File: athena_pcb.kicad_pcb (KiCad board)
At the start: 2 copper layers, 41.6 x 23.5 mm, 34 parts, among them J2 Conn_01x04, SW1 SW_Push, U1 NRF5340-QKAA-R7, U2 BME280, Y1 32MHz, Y2 32.768kHz

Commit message: Polishing layout
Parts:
- added TP3: TestPoint, TestPoint:TestPoint_Pad_D1.0mm, F.Cu at (99.0, 96.8)
- added TP4: TestPoint, TestPoint:TestPoint_Pad_D1.0mm, F.Cu at (108.8, 96.8)
- moved R1 1.78 mm to (102.6, 92.9)
- moved D1 1.77 mm to (103.1, 91.5)
- moved C9 0.30 mm to (118.0, 95.4)
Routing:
- net VDD: track 165.1 -> 187.1 mm, vias 2 -> 3
- net GND: track 32.2 -> 40.2 mm, vias 15 -> 21
- net unconnected-(U1D-P1.08-PadAL23): track 1.25 -> 0.00 mm
- net /P0.02: track 21.0 -> 22.2 mm
- net /SCK_SCL: track 23.9 -> 24.7 mm
- net /P0.03: track 10.7 -> 10.1 mm
- net /CSB: track 23.2 -> 23.8 mm
- net /SDI_SDA: track 23.3 -> 23.9 mm
- net /SDO: track 25.3 -> 25.8 mm

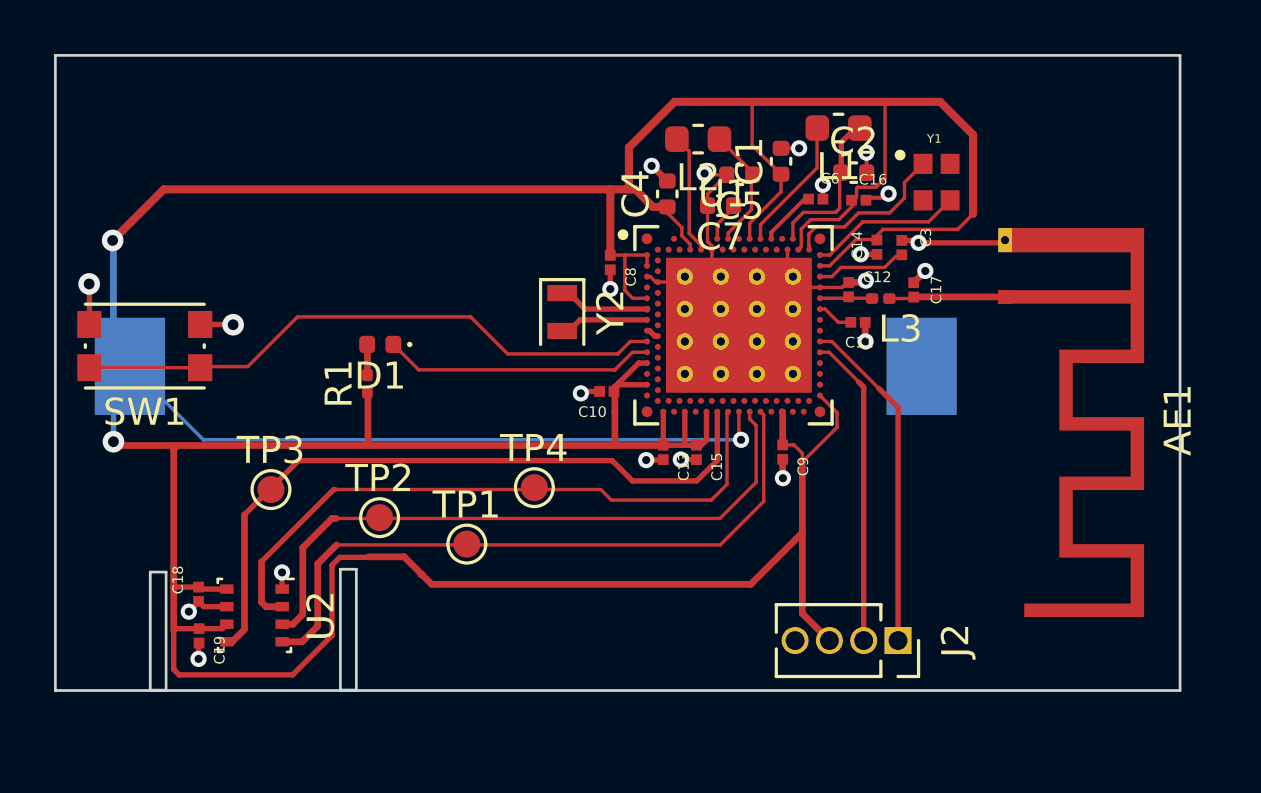
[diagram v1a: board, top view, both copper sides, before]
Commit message: Updated Header pinout, added ground pours to PCB
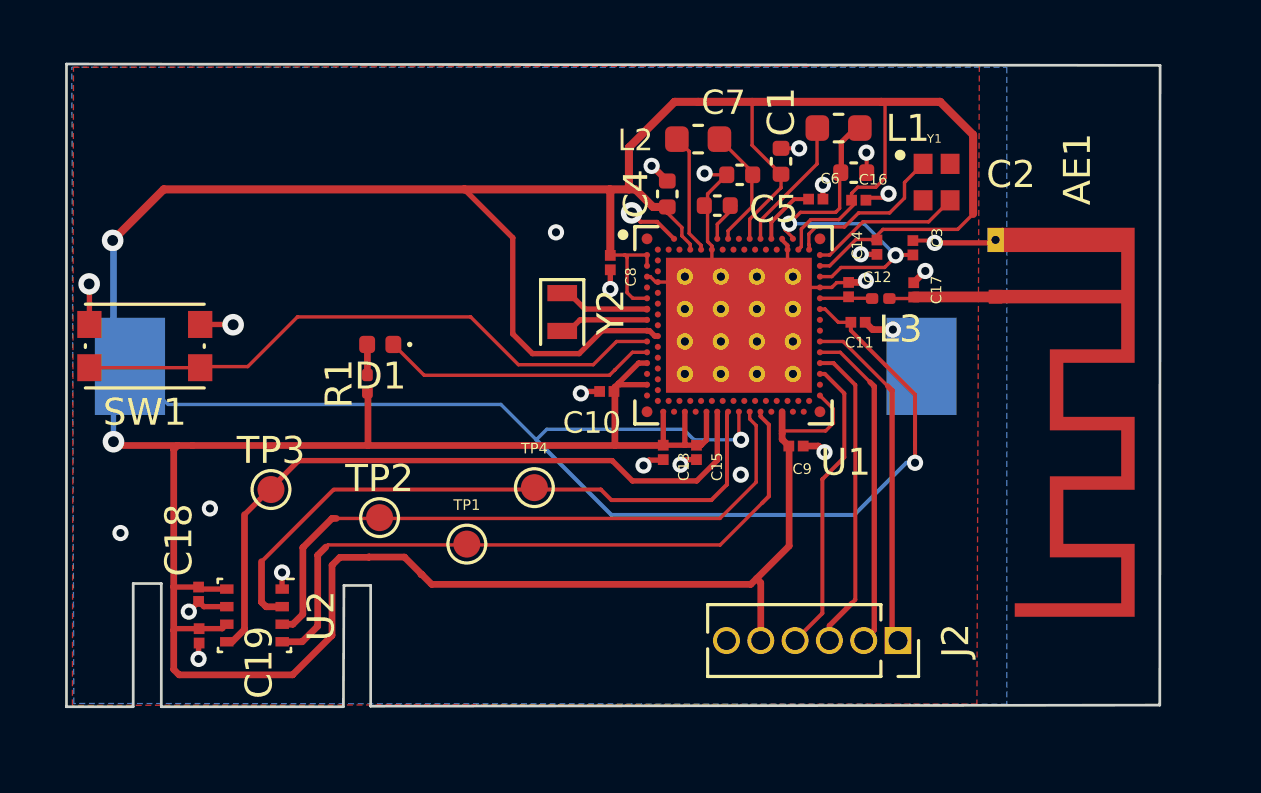
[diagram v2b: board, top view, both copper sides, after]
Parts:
- J2: footprint Connector_PinSocket_1.27mm:PinSocket_1x04_P1.27mm_Vertical -> Connector_PinSocket_1.27mm:PinSocket_1x06_P1.27mm_Vertical
- moved C9 0.54 mm to (118.4, 95.2), turned to 0 degrees
- moved C3 0.41 mm to (122.8, 87.9)
- moved AE1 0.35 mm to (125.8, 89.7)
- moved C7 0.12 mm to (115.5, 86.3)
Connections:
- J2 pad 3: VDD -> /RESETN
- J2 pad 4: GND -> /P0.28
- U1 pad AC31: unconnected-(U1B-~{RESET}-PadAC31) -> /RESETN
- U1 pad AE31: unconnected-(U1C-P0.28/AIN7-PadAE31) -> /P0.28
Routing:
- net VDD: track 187.1 -> 218.6 mm, vias 3 -> 4
- net /RESETN: track 0.00 -> 11.5 mm
- net /P0.28: track 0.00 -> 11.1 mm
- net Net-(U1A-DECR): track 8.84 -> 14.3 mm, vias 0 -> 2
- net GND: track 40.2 -> 43.3 mm, vias 21 -> 26
- net /SWDIO: track 11.5 -> 12.1 mm
- added copper zone on B.Cu, net GND
- added copper zone on F.Cu, net GND
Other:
- board size 41.6 x 23.5 mm -> 40.5 x 23.8 mm

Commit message: Changes from the review
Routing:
- net VDD: track 218.6 -> 167.2 mm, vias 4 -> 7
- net GND: track 43.3 -> 38.8 mm, vias 26 -> 25

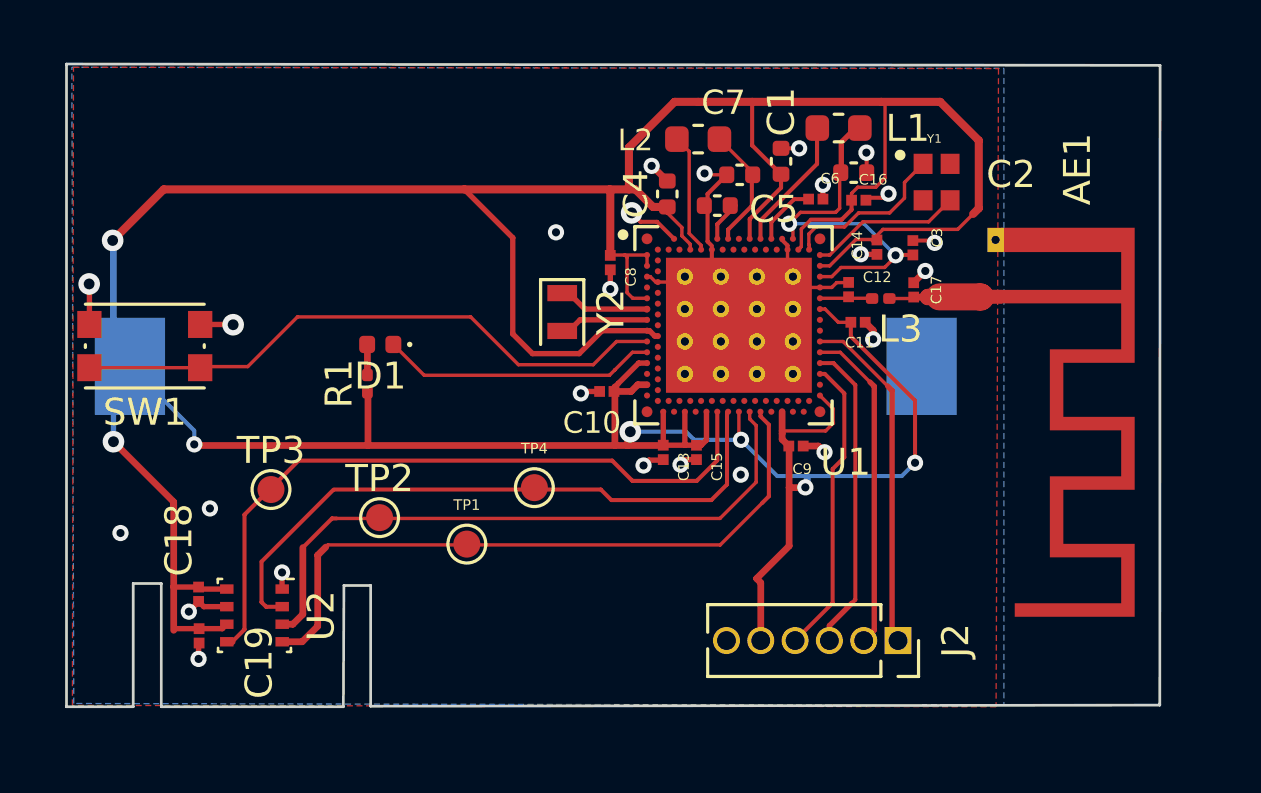
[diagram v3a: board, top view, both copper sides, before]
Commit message: Added items in the BOM
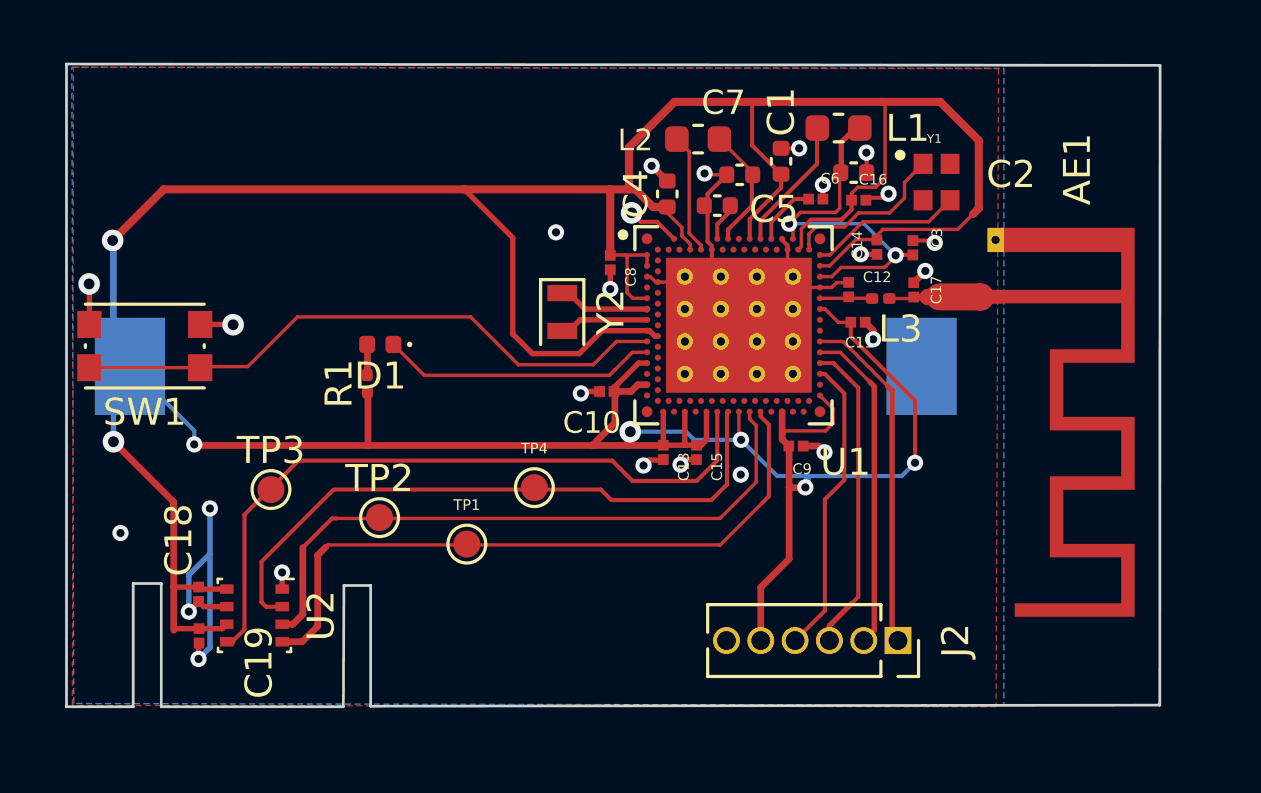
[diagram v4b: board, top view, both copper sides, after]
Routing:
- net GND: track 38.8 -> 47.0 mm
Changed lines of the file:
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@@
       (net 1 "VDD") (pinfunction "+") (pintype "passive"))
     (pad "2" smd rect (at 14.65 0 180) (size 2.6 3.6) (layers "B.Cu" "B.Paste" "B.Mask")
-      (net 2 "GND") (pinfunction "-") (pintype "passive"))
+      (net 2 "GND") (pinfunction "-") (pintype "passive") (zone_connect 1))
     (model "${KICAD6_3DMODEL_DIR}/Battery.3dshapes/BatteryHolder_Keystone_1060_1x2032.wrl"
       (offset (xyz 0 0 0))
@@
   (segment (start 111.2695 90.94) (end 110.4195 91.79) (width 0.2) (layer "F.Cu") (net 1))
   (segment (start 120.5 86.46283) (end 120.5 86.11) (width 0.1524) (layer "F.Cu") (net 1))
+  (segment (start 117.14 102.41) (end 117.14 100.44) (width 0.25) (layer "F.Cu") (net 1))
   (segment (start 111.57 88.154) (end 111.57 85.73) (width 0.3) (layer "F.Cu") (net 1))
   (segment (start 112.4 89.74) (end 112.19 89.53) (width 0.127) (layer "F.Cu") (net 1))
@@
   (segment (start 120.73 85.63) (end 121.4 85.63) (width 0.127) (layer "F.Cu") (net 1))
   (segment (start 114.33 93.94) (end 114.33 95.18) (width 0.2) (layer "F.Cu") (net 1))
-  (segment (start 117.14 102.41) (end 117.14 100.27) (width 0.25) (layer "F.Cu") (net 1))
   (segment (start 112.93 92.14) (end 112.62 92.14) (width 0.2) (layer "F.Cu") (net 1))
   (segment (start 118.64 87.18) (end 118.99 86.83) (width 0.127) (layer "F.Cu") (net 1))
@@
   (segment (start 112.93 88.14) (end 112.11 88.14) (width 0.127) (layer "F.Cu") (net 1))
   (segment (start 117.89 85.15) (end 116.82 84.08) (width 0.1524) (layer "F.Cu") (net 1))
-  (segment (start 118.19 98.91) (end 118.19 96.75) (width 0.25) (layer "F.Cu") (net 1))
   (segment (start 113.22 91.14) (end 113.02 90.94) (width 0.2) (layer "F.Cu") (net 1))
   (segment (start 95.04 85.71) (end 106.17 85.71) (width 0.3) (layer "F.Cu") (net 1))
@@
   (segment (start 121.6 82.47) (end 116.82 82.47) (width 0.3) (layer "F.Cu") (net 1))
   (segment (start 106.17 85.71) (end 111.55 85.71) (width 0.3) (layer "F.Cu") (net 1))
-  (segment (start 117.14 100.27) (end 116.985 100.115) (width 0.25) (layer "F.Cu") (net 1))
   (segment (start 107.96 87.5) (end 106.17 85.71) (width 0.2) (layer "F.Cu") (net 1))
   (segment (start 120.5 85.86) (end 120.73 85.63) (width 0.127) (layer "F.Cu") (net 1))
@@
   (segment (start 95.41 97.28) (end 93.18 95.05) (width 0.25) (layer "F.Cu") (net 1))
   (segment (start 102.6 93.24) (end 102.58 93.22) (width 0.25) (layer "F.Cu") (net 1))
+  (segment (start 111.74 93.02) (end 111.74 94.35) (width 0.25) (layer "F.Cu") (net 1))
   (segment (start 119.82 94.35) (end 119.83 94.36) (width 0.127) (layer "F.Cu") (net 1))
   (segment (start 116.82 84.08) (end 116.82 82.47) (width 0.1524) (layer "F.Cu") (net 1))
   (segment (start 119.33 88.54) (end 119.69 88.54) (width 0.127) (layer "F.Cu") (net 1))
   (segment (start 114.94 95.18) (end 114.76 95.18) (width 0.2) (layer "F.Cu") (net 1))
-  (segment (start 111.74 95.18) (end 111.73 95.19) (width 0.127) (layer "F.Cu") (net 1))
   (segment (start 95.42 100.43) (end 95.41 100.42) (width 0.2) (layer "F.Cu") (net 1))
   (segment (start 121.664 87.19) (end 124.43 87.19) (width 0.127) (layer "F.Cu") (net 1))
@@
   (segment (start 116.73 86.81) (end 116.73 87.54) (width 0.1524) (layer "F.Cu") (net 1))
   (segment (start 93.32 95.19) (end 93.18 95.05) (width 0.25) (layer "F.Cu") (net 1))
-  (segment (start 111.74 93.02) (end 111.74 93.98) (width 0.25) (layer "F.Cu") (net 1))
   (segment (start 114.22 87.430111) (end 114.22 87.12) (width 0.127) (layer "F.Cu") (net 1))
   (segment (start 112.19 89.53) (end 112.19 88.22) (width 0.127) (layer "F.Cu") (net 1))
@@
   (segment (start 112.19 88.22) (end 112.11 88.14) (width 0.127) (layer "F.Cu") (net 1))
   (segment (start 95.41 102.03) (end 95.41 100.42) (width 0.25) (layer "F.Cu") (net 1))
+  (segment (start 117.14 100.44) (end 118.19 99.39) (width 0.25) (layer "F.Cu") (net 1))
   (segment (start 93.18 95.05) (end 93.18 95.29) (width 0.2) (layer "F.Cu") (net 1))
   (segment (start 122.85 93.53) (end 122.85 95.83) (width 0.15) (layer "F.Cu") (net 1))
@@
   (segment (start 120.5 86.11) (end 120.5 85.86) (width 0.127) (layer "F.Cu") (net 1))
   (segment (start 111.55 85.71) (end 112.5 85.71) (width 0.3) (layer "F.Cu") (net 1))
+  (segment (start 111.74 94.35) (end 110.9 95.19) (width 0.25) (layer "F.Cu") (net 1))
   (segment (start 97.375 101.805) (end 97.21 101.97) (width 0.2) (layer "F.Cu") (net 1))
   (segment (start 119.33 90.14) (end 119.52 90.14) (width 0.127) (layer "F.Cu") (net 1))
-  (segment (start 111.74 93.98) (end 111.74 95.18) (width 0.25) (layer "F.Cu") (net 1))
   (segment (start 117.93 94.962) (end 117.93 94.75) (width 0.25) (layer "F.Cu") (net 1))
   (segment (start 102.6 95.19) (end 96.1 95.19) (width 0.25) (layer "F.Cu") (net 1))
@@
   (segment (start 95.41 100.42) (end 95.41 97.42) (width 0.25) (layer "F.Cu") (net 1))
   (segment (start 111.87 92.89) (end 111.74 93.02) (width 0.2) (layer "F.Cu") (net 1))
-  (segment (start 116.985 100.115) (end 118.19 98.91) (width 0.25) (layer "F.Cu") (net 1))
+  (segment (start 118.19 99.39) (end 118.19 96.75) (width 0.25) (layer "F.Cu") (net 1))
   (segment (start 96.35 101.97) (end 95.47 101.97) (width 0.2) (layer "F.Cu") (net 1))
   (segment (start 116.33 94.9) (end 116.41 94.98) (width 0.127) (layer "F.Cu") (net 1))
@@
   (via (at 99.42 99.89) (size 0.6) (drill 0.3) (layers "F.Cu" "B.Cu") (net 2))
   (via (at 118.56 84.19) (size 0.6) (drill 0.3) (layers "F.Cu" "B.Cu") (net 2))
+  (segment (start 95.97 99.98) (end 96.75 99.2) (width 0.2) (layer "B.Cu") (net 2))
+  (segment (start 96.33 103.09) (end 96.75 102.67) (width 0.2) (layer "B.Cu") (net 2))
+  (segment (start 96.75 102.67) (end 96.75 97.52) (width 0.2) (layer "B.Cu") (net 2))
+  (segment (start 95.97 101.34) (end 95.97 99.98) (width 0.2) (layer "B.Cu") (net 2))
   (segment (start 120.12 85.07) (end 120.1 85.09) (width 0.2) (layer "F.Cu") (net 3))
   (segment (start 121.725 88.6) (end 120.11 88.6) (width 0.127) (layer "F.Cu") (net 3))
@@
   (segment (start 112.39 91.74) (end 111.74 92.39) (width 0.127) (layer "F.Cu") (net 44))
   (segment (start 111.74 92.39) (end 111.73 92.4) (width 0.127) (layer "F.Cu") (net 44))
-  (segment (start 119.83 92.14) (end 120.64 92.95) (width 0.15) (layer "F.Cu") (net 53))
+  (segment (start 119.68 101.86) (end 119.68 102.41) (width 0.2) (layer "F.Cu") (net 53))
+  (segment (start 120.75 93.06) (end 120.75 100.79) (width 0.15) (layer "F.Cu") (net 53))
+  (segment (start 120.75 100.79) (end 120.51 101.03) (width 0.15) (layer "F.Cu") (net 53))
+  (segment (start 119.83 92.14) (end 120.75 93.06) (width 0.15) (layer "F.Cu") (net 53))
   (segment (start 119.33 92.14) (end 119.83 92.14) (width 0.15) (layer "F.Cu") (net 53))
-  (segment (start 119.68 101.86) (end 119.68 102.41) (width 0.2) (layer "F.Cu") (net 53))
   (segment (start 120.51 101.03) (end 119.68 101.86) (width 0.2) (layer "F.Cu") (net 53))
-  (segment (start 120.64 100.9) (end 120.51 101.03) (width 0.15) (layer "F.Cu") (net 53))
-  (segment (start 120.64 92.95) (end 120.64 100.9) (width 0.15) (layer "F.Cu") (net 53))
+  (segment (start 120.233 96.467) (end 119.51 97.19) (width 0.15) (layer "F.Cu") (net 54))
+  (segment (start 119.51 101.31) (end 118.41 102.41) (width 0.15) (layer "F.Cu") (net 54))
+  (segment (start 119.33 92.54) (end 119.51 92.54) (width 0.15) (layer "F.Cu") (net 54))
+  (segment (start 120.233 93.263) (end 120.233 96.467) (width 0.15) (layer "F.Cu") (net 54))
   (segment (start 119.51 92.54) (end 120.233 93.263) (width 0.15) (layer "F.Cu") (net 54))
-  (segment (start 119.33 92.54) (end 119.51 92.54) (width 0.15) (layer "F.Cu") (net 54))
-  (segment (start 119.8 96.06) (end 119.8 101.02) (width 0.15) (layer "F.Cu") (net 54))
-  (segment (start 120.233 95.627) (end 119.8 96.06) (width 0.15) (layer "F.Cu") (net 54))
-  (segment (start 119.8 101.02) (end 118.41 102.41) (width 0.15) (layer "F.Cu") (net 54))
-  (segment (start 120.233 93.263) (end 120.233 95.627) (width 0.15) (layer "F.Cu") (net 54))
+  (segment (start 119.51 97.19) (end 119.51 101.31) (width 0.15) (layer "F.Cu") (net 54))
   (segment (start 108.17 92.2) (end 106.4 90.43) (width 0.127) (layer "F.Cu") (net 72))
   (segment (start 99.99 90.43) (end 98.15 92.27) (width 0.127) (layer "F.Cu") (net 72))
@@
     (polygon
       (pts
-        (xy 95.14 100.23)
-        (xy 101.51 100.23)
+        (xy 95.15 99.76)
+        (xy 101.52 99.76)
         (xy 101.51 104.65)
         (xy 95.12 104.63)

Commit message: Cleaned Track not connected Warnings
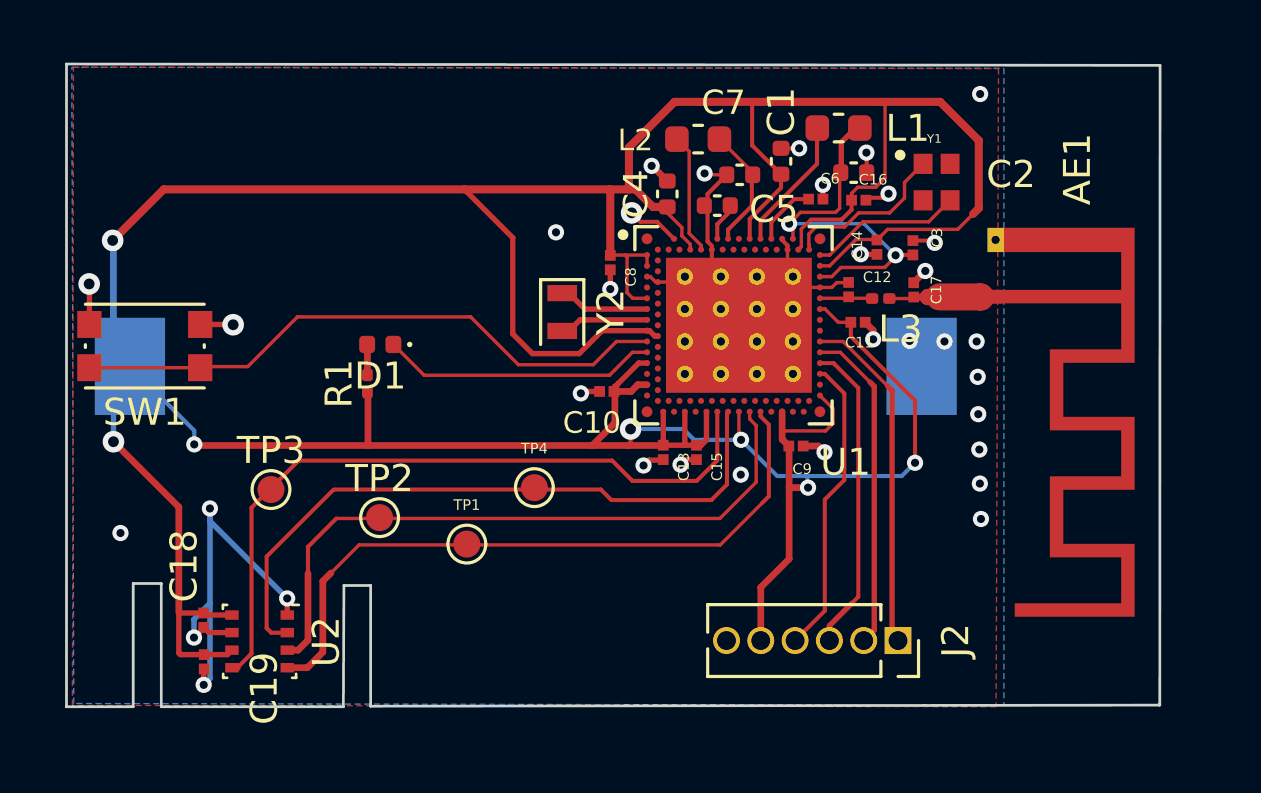
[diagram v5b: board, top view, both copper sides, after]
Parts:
- moved C18 0.98 mm to (96.5, 101.7)
- moved C19 0.98 mm to (96.5, 103.2)
- moved U2 0.98 mm to (98.6, 102.4)
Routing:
- net GND: track 47.0 -> 51.3 mm, vias 25 -> 34
- net /CSB: track 23.7 -> 24.6 mm
- net /SDO: track 25.8 -> 26.7 mm
- net /SDI_SDA: track 23.9 -> 24.7 mm
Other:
- board text added: "Athena MK1"
